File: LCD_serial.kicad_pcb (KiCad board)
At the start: 2 copper layers, 5 parts, among them P1 CONN_01X05, U1 74LS164

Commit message: Starting on the PCB layout
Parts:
- DS1: footprint Display:LCD-016N002L -> Pin_Headers:Pin_Header_Straight_1x14
- P1, R1: moved to B.Cu
- moved U1 36.8 mm to (166.4, 137.2), turned to 180 degrees
- moved D1 31.6 mm to (154.9, 135.9), turned to 90 degrees
- moved P1 20.8 mm to (166.4, 115.6)
- moved R1 14.6 mm to (154.9, 118.1)
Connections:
- net GND renamed Net-(DS1-Pad1)
- net VCC renamed Net-(DS1-Pad2)
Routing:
- net Net-(DS1-Pad2): track 0.00 -> 18.0 mm
- net Net-(DS1-Pad1): track 0.00 -> 18.0 mm

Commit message: layout progress
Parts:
- P1: value CONN_01X05 -> CONN_01X05_GJ
- moved U1 33.0 mm to (157.5, 105.4), turned to 0 degrees
- moved DS1 32.2 mm to (148.6, 137.2), turned to 180 degrees
- moved D1 20.4 mm to (153.7, 115.6), turned to 270 degrees
- moved P1 11.7 mm to (163.8, 127.0), turned to 180 degrees
- moved R1 11.4 mm to (154.9, 129.5)
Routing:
- net Net-(DS1-Pad2): track 18.0 -> 51.1 mm
- net Net-(DS1-Pad12): track 0.00 -> 32.6 mm
- net Net-(DS1-Pad13): track 0.00 -> 29.3 mm
- net Net-(DS1-Pad14): track 0.00 -> 26.8 mm
- net Net-(DS1-Pad3): track 0.00 -> 15.2 mm
- net Net-(DS1-Pad1): track 18.0 -> 32.8 mm, vias 0 -> 2
- net Net-(D1-Pad2): track 0.00 -> 9.72 mm
- net Net-(P1-Pad2): track 0.00 -> 6.89 mm
- net Net-(P1-Pad1): track 0.00 -> 6.88 mm

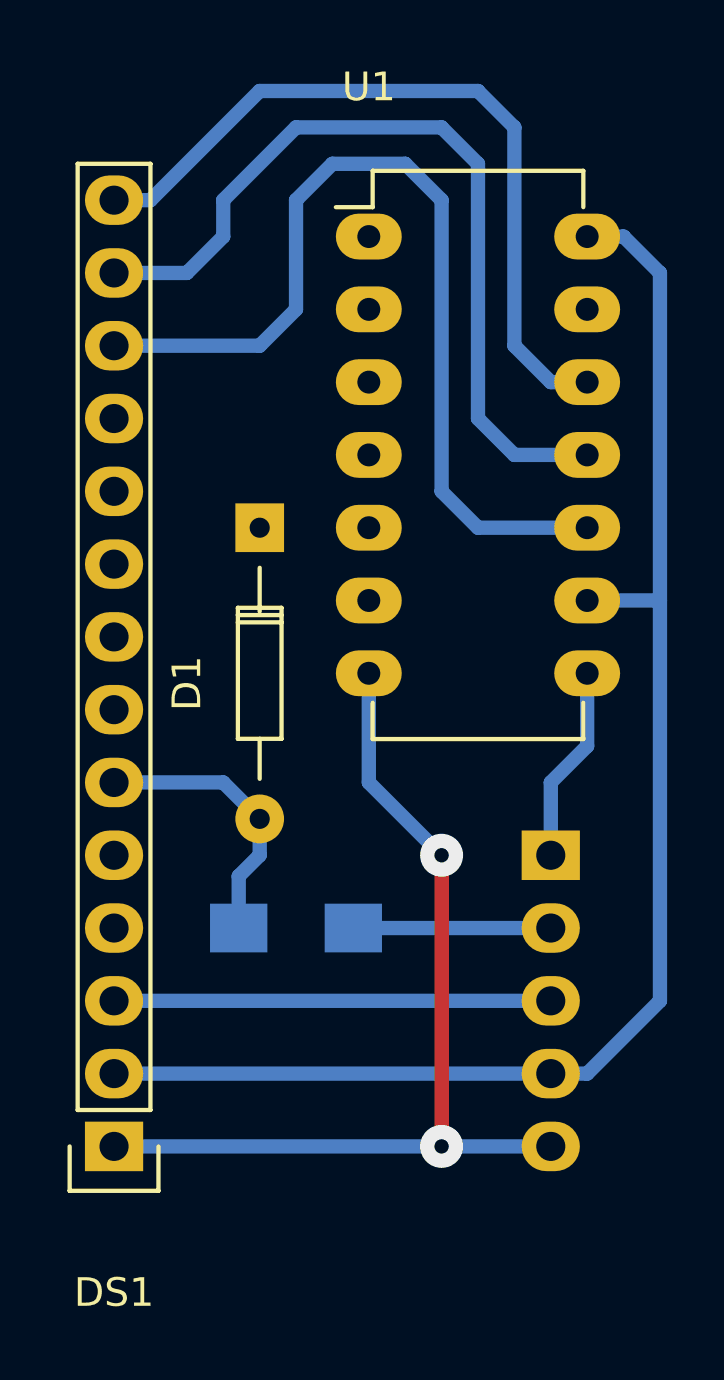
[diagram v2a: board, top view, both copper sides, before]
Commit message: Fabricated version of board
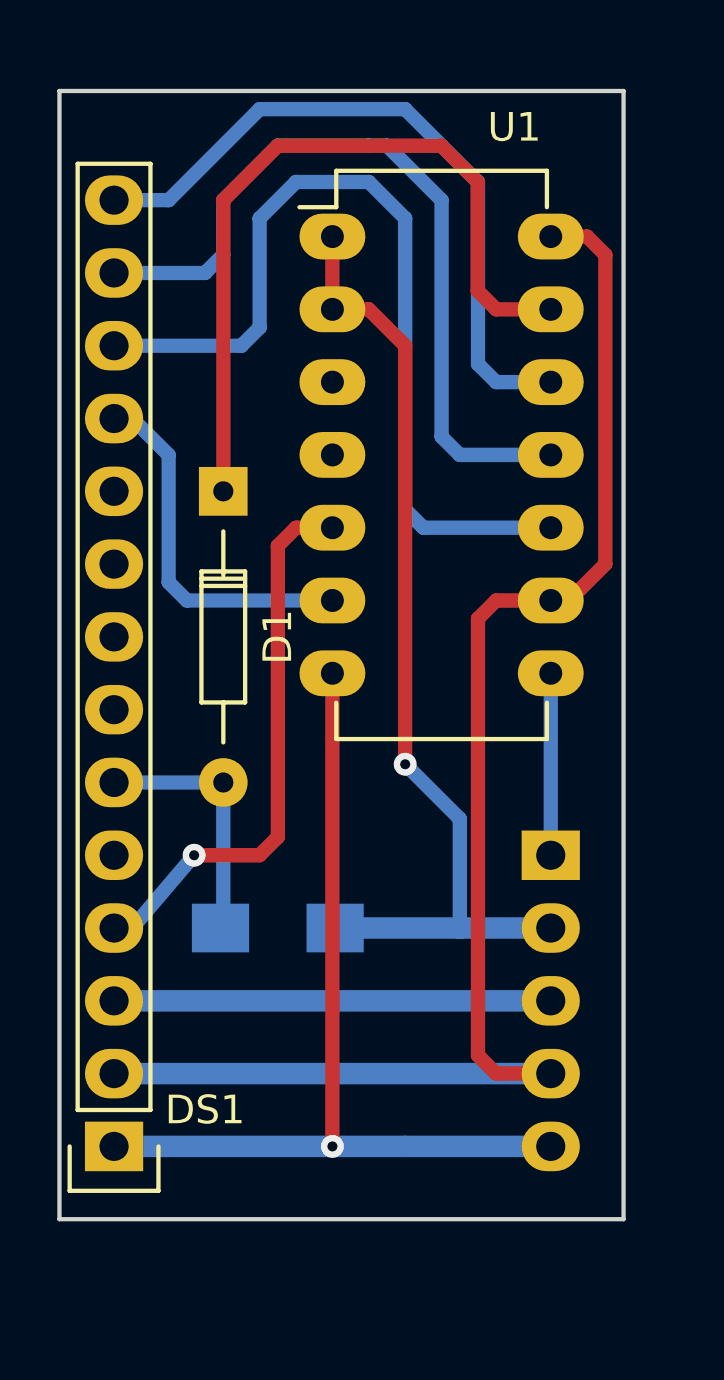
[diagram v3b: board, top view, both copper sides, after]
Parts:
- moved D1 1.80 mm to (152.4, 114.3)
- moved U1 1.27 mm to (156.2, 105.4)
- moved R1 0.63 mm to (154.3, 129.5)
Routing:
- net Net-(P1-Pad2): track 6.89 -> 34.2 mm, vias 0 -> 1
- net Net-(D1-Pad1): track 0.00 -> 27.0 mm
- net Net-(DS1-Pad4): track 0.00 -> 19.5 mm, vias 0 -> 1
- net Net-(DS1-Pad11): track 0.00 -> 12.9 mm
- net Net-(DS1-Pad14): track 26.8 -> 24.2 mm
- net Net-(DS1-Pad13): track 29.3 -> 27.5 mm
- net Net-(DS1-Pad12): track 32.6 -> 30.8 mm
- net Net-(DS1-Pad1): track 32.8 -> 31.8 mm, vias 2 -> 1
- net Net-(D1-Pad2): track 9.72 -> 8.93 mm
- net Net-(P1-Pad1): track 6.88 -> 6.35 mm
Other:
- board outline added: 19.7 x 39.4 mm
